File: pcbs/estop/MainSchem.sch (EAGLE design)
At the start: 30 parts, among them J1 XT60-M, J2 XT60-M, J3 XT60-M, J4 XT60-M, J5 XT60-M, Q1 FDBL9401-F085, Q2 FDBL9401-F085, U1 FAN3100T, U2 FAN3100T

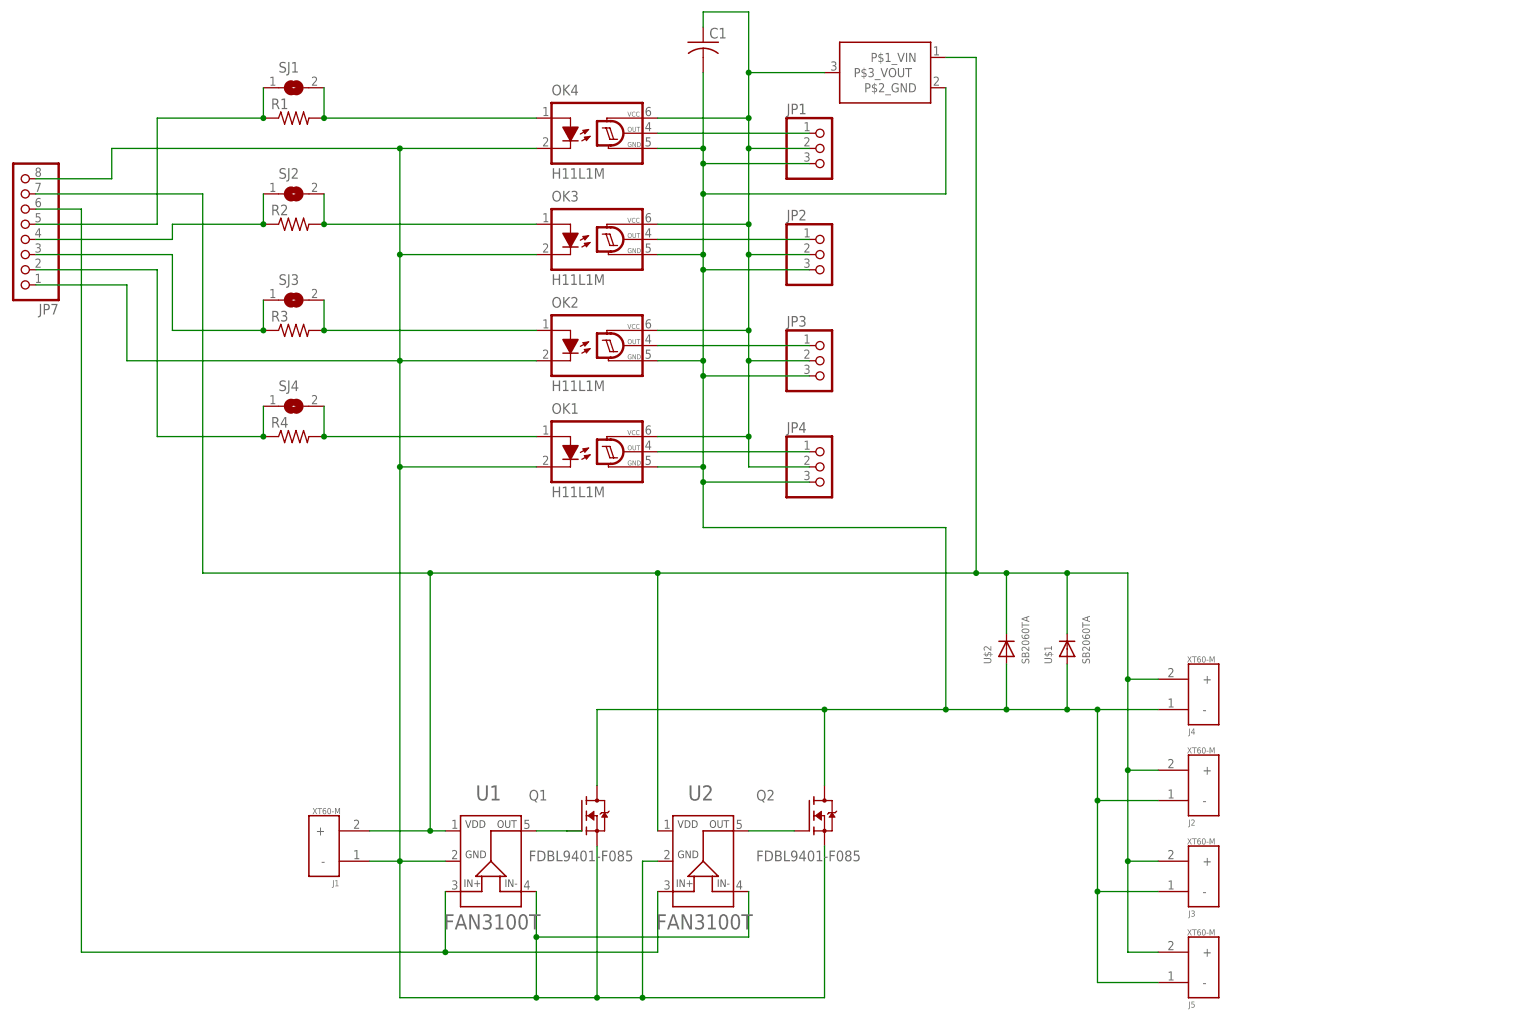
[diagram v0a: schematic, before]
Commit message: Made improvements to e-stop layout and schematic. Added high-current pads.
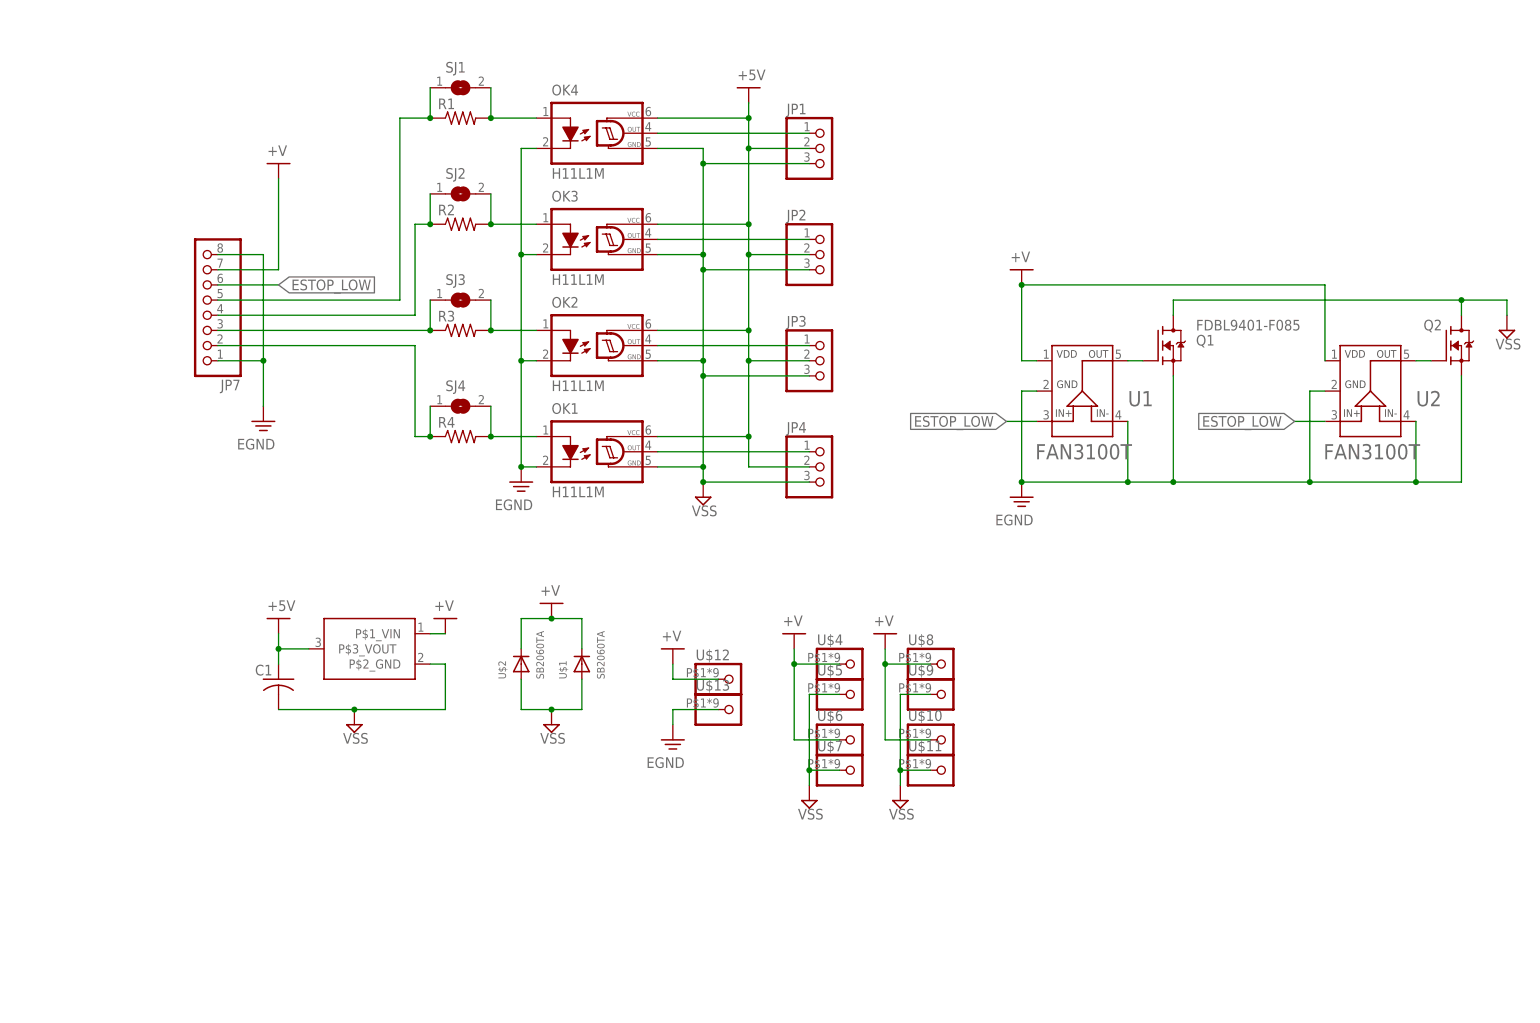
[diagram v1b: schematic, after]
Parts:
- removed J1, J2, J3, J4, J5: XT60-M, XT60-M:XT60-M
- added U$10, U$11, U$12, U$13, U$4, U$5, U$6, U$7, U$8, U$9: HIGH_CURRENT_WIRE_PAD, HighCurrentTransistorAndDriver:HIGH_CURRENT_WIRE_PAD
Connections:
- net N$8 renamed ESTOP_LOW
- removed net BAT+: J1.+, J2.+, J3.+, J4.+, J5.+, JP7.7, U$1.C, U$2.C, U$3.P$1_VIN, U1.VDD, U2.VDD
- removed net ESC_GND: C1.2, J2.-, J3.-, J4.-, J5.-, JP1.3, JP2.3, JP3.3, JP4.3, OK1.GND, OK2.GND, OK3.GND, OK4.GND, Q1.D, Q2.D, U$1.A, U$2.A, U$3.P$2_GND
- removed net ESC_SIDE_5V: C1.1, JP1.2, JP2.2, JP3.2, JP4.2, OK1.VCC, OK2.VCC, OK3.VCC, OK4.VCC, U$3.P$3_VOUT
- removed net TRUE_GND_BATT-: J1.-, JP7.1, JP7.8, OK1.C, OK2.C, OK3.C, OK4.C, Q1.S, Q2.S, U1.GND, U1.IN-, U2.GND, U2.IN-
- new net +V: C1.1, JP1.2, JP2.2, JP3.2, JP4.2, JP7.7, OK1.VCC, OK2.VCC, OK3.VCC, OK4.VCC, U$1.C, U$10.1, U$12.1, U$2.C, U$3.P$1_VIN, U$3.P$3_VOUT, U$4.1, U$6.1, U$8.1, U1.VDD, U2.VDD
- new net EGND: JP7.1, JP7.8, OK1.C, OK2.C, OK3.C, OK4.C, Q1.S, Q2.S, U$13.1, U1.GND, U1.IN-, U2.GND, U2.IN-
- new net VSS: C1.2, JP1.3, JP2.3, JP3.3, JP4.3, OK1.GND, OK2.GND, OK3.GND, OK4.GND, Q1.D, Q2.D, U$1.A, U$11.1, U$2.A, U$3.P$2_GND, U$5.1, U$7.1, U$9.1
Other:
- moved on the sheet: C1, JP7, Q1, Q2, R1, R2, R3, R4, SJ1, SJ2, SJ3, SJ4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

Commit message: E-stop board layout appears complete.
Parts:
- added U$14, U$15: HIGH_CURRENT_WIRE_PAD, HighCurrentTransistorAndDriver:HIGH_CURRENT_WIRE_PAD
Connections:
- removed net +V: C1.1, JP1.2, JP2.2, JP3.2, JP4.2, JP7.7, OK1.VCC, OK2.VCC, OK3.VCC, OK4.VCC, U$1.C, U$10.1, U$12.1, U$2.C, U$3.P$1_VIN, U$3.P$3_VOUT, U$4.1, U$6.1, U$8.1, U1.VDD, U2.VDD
- new net +5V: C1.1, JP1.2, JP2.2, JP3.2, JP4.2, OK1.VCC, OK2.VCC, OK3.VCC, OK4.VCC, U$3.P$3_VOUT
- new net V+: JP7.7, U$1.C, U$10.1, U$12.1, U$15.1, U$2.C, U$3.P$1_VIN, U$4.1, U$6.1, U$8.1, U1.VDD, U2.VDD
- net EGND: now also U$14.1
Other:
- moved on the sheet: U$12, U$13

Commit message: Increased e-stop <-> interposer ribbon cable drill size to make soldering the ribbon cable easier in future versions.
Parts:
- JP7: device pinhead:PINHD-1X8 -> HighCurrentTransistorAndDriver:PINHD-1X8_RIBBONCABLE
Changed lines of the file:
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@@
 <part name="R3" library="adafruit" library_urn="urn:adsk.eagle:library:420" deviceset="R-US_" device="0204/7" package3d_urn="urn:adsk.eagle:package:6240596/1"/>
 <part name="R4" library="adafruit" library_urn="urn:adsk.eagle:library:420" deviceset="R-US_" device="0204/7" package3d_urn="urn:adsk.eagle:package:6240596/1"/>
-<part name="JP7" library="pinhead" library_urn="urn:adsk.eagle:library:325" deviceset="PINHD-1X8" device="" package3d_urn="urn:adsk.eagle:package:22409/2"/>
+<part name="JP7" library="HighCurrentTransistorAndDriver" deviceset="PINHD-1X8_RIBBONCABLE" device="" package3d_urn="urn:adsk.eagle:package:22409/2"/>
 <part name="SUPPLY1" library="Power_Symbols" library_urn="urn:adsk.eagle:library:16502351" deviceset="EGND" device=""/>
 <part name="SUPPLY2" library="Power_Symbols" library_urn="urn:adsk.eagle:library:16502351" deviceset="EGND" device=""/>
